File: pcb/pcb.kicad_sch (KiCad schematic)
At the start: 4 parts

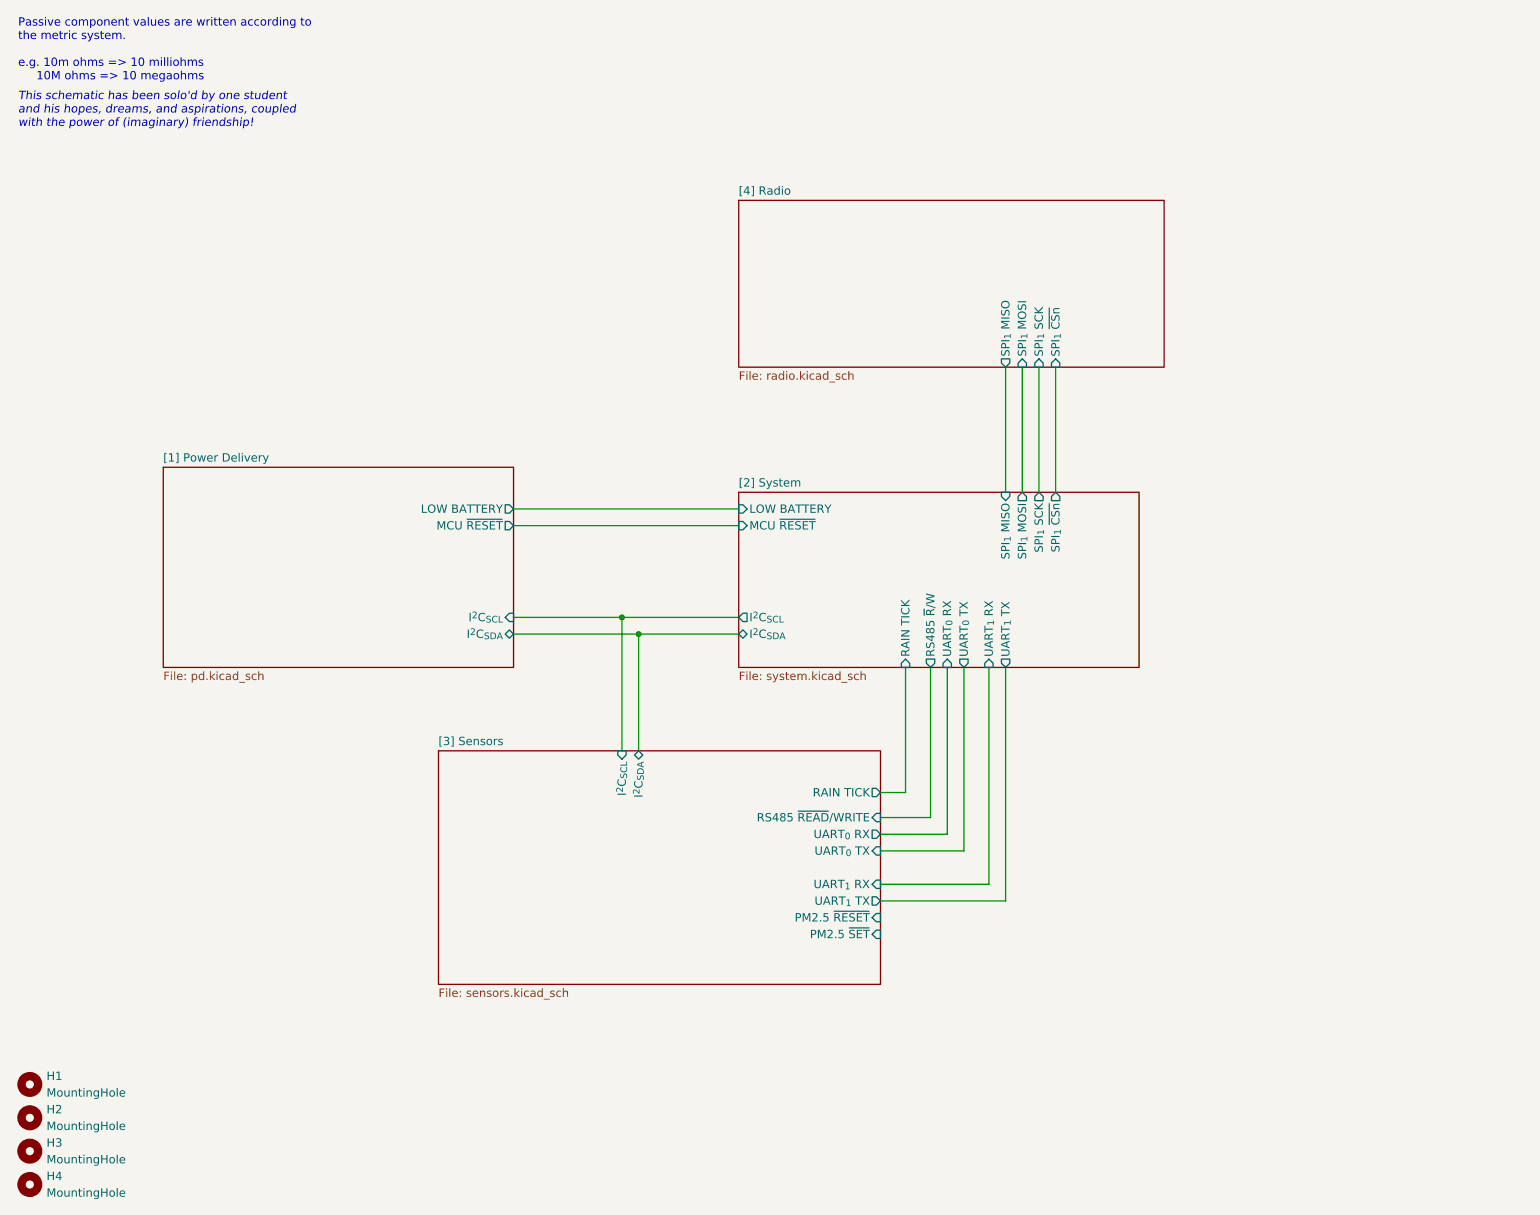
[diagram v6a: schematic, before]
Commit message: feat: added documentation, updated page information
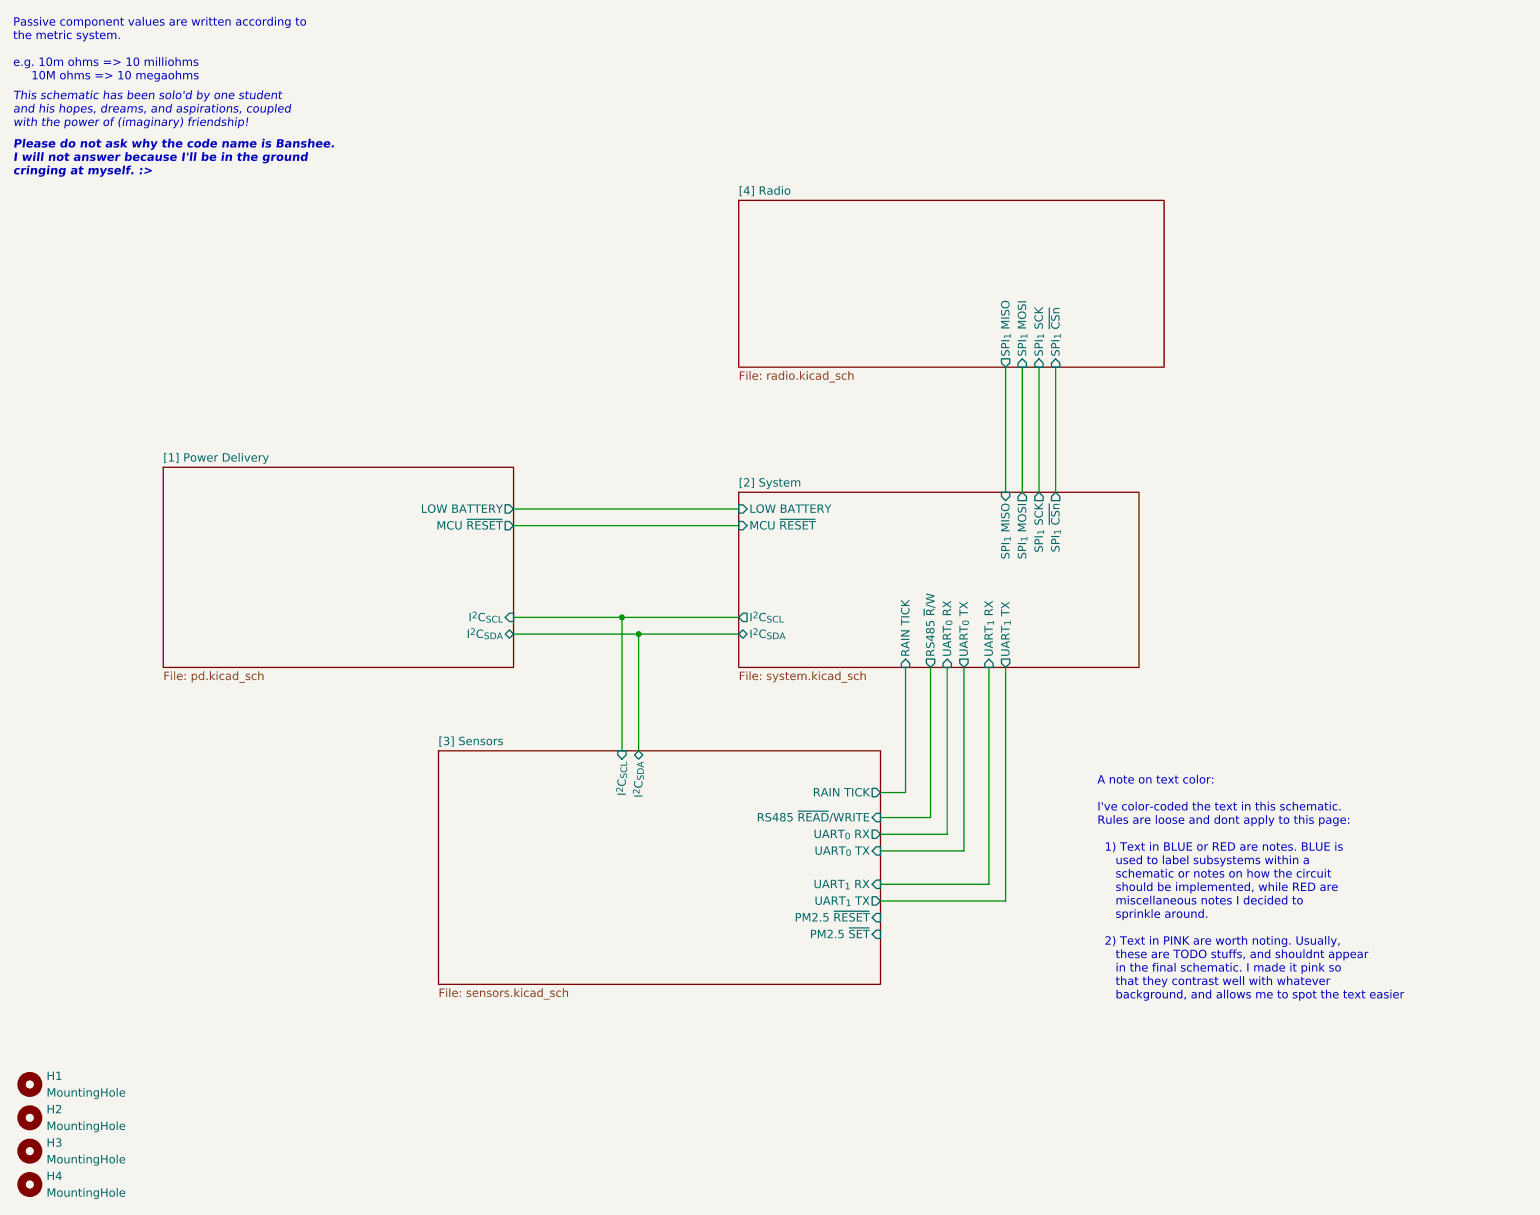
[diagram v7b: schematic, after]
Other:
- note added: "A note on text color: I've color-coded the text in this schematic. Rules are loose and dont apply to this page: 1) Text in BLUE or RED are notes. BLUE is used to label subsystems within a schematic or notes on how the circuit should be implemented, while RED are miscellaneous notes I decided to sprinkle around. 2) Text in PINK are worth noting. Usually, these are TODO stuffs, and shouldnt appear 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"
- note added: "Please do not ask why the code name is Banshee. I will not answer because I'll be in the ground cringing at myself. :>"
- title: Banshee Power Delivery System -> Banshee System Overview
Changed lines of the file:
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@@
 	(paper "A4")
 	(title_block
-		(title "Banshee Power Delivery System")
+		(title "Banshee System Overview")
 		(date "2026-02-26")
 		(rev "1")
@@
 	(text "This schematic has been solo'd by one student\nand his hopes, dreams, and aspirations, coupled\nwith the power of (imaginary) friendship!"
 		(exclude_from_sim no)
-		(at 14.732 29.464 0)
+		(at 13.97 29.464 0)
 		(effects
 			(font
@@
 	(text "Passive component values are written according to\nthe metric system.\n\ne.g. 10m ohms => 10 milliohms\n     10M ohms => 10 megaohms"
 		(exclude_from_sim no)
-		(at 14.732 20.32 0)
+		(at 13.97 20.32 0)
 		(effects
 			(font
@@
 		)
 	)
+	(text "Please do not ask why the code name is Banshee.\nI will not answer because I'll be in the ground\ncringing at myself. :>"
+		(exclude_from_sim no)
+		(at 13.97 36.83 0)
+		(effects
+			(font
+				(size 1.27 1.27)
+				(thickness 0.254)
+				(bold yes)
+				(italic yes)
+				(color 132 0 0 1)
+			)
+			(justify left)
+		)
+	)
+	(text "A note on text color:\n\nI've color-coded the text in this schematic.\nRules are loose and dont apply to this page:\n\n  1) Text in BLUE or RED are notes. BLUE is\n     used to label subsystems within a\n     schematic or notes on how the circuit\n     should be implemented, while RED are \n     miscellaneous notes I decided to \n     sprinkle around.\n\n  2) Text in PINK are worth noting. Usually,\n     these are TODO stuffs, and shouldnt appear\n     in the final schematic. I made it pink so\n     that they contrast well with whatever\n     background, and allows me to spot the text easier"
+		(exclude_from_sim no)
+		(at 179.07 165.1 0)
+		(effects
+			(font
+				(size 1.27 1.27)
+			)
+			(justify left bottom)
+		)
+	)

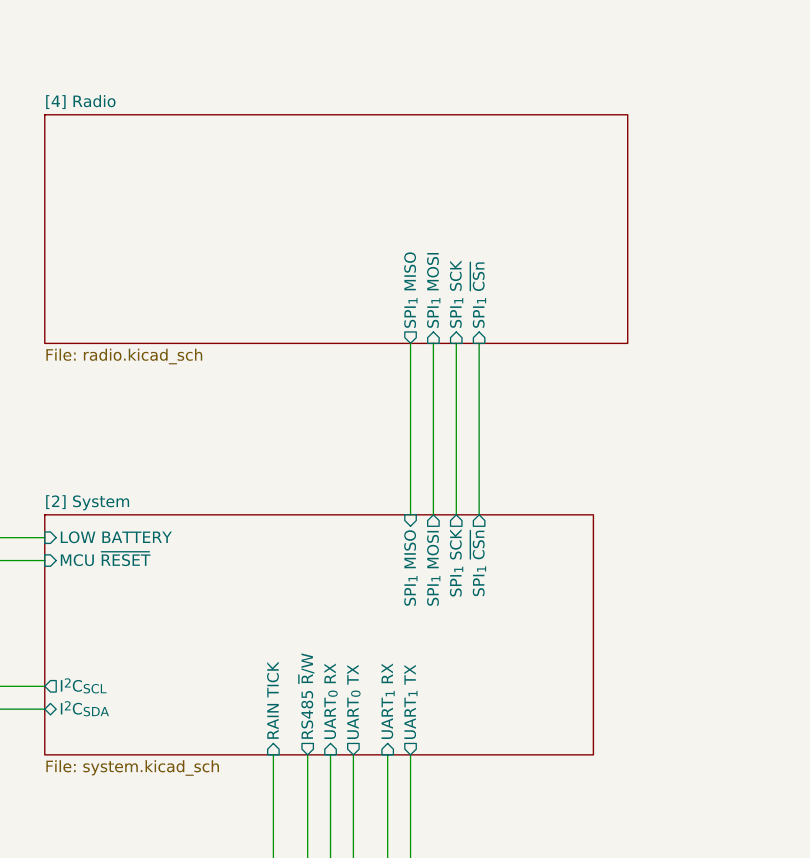
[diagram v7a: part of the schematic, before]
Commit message: feat: sx1278 radio
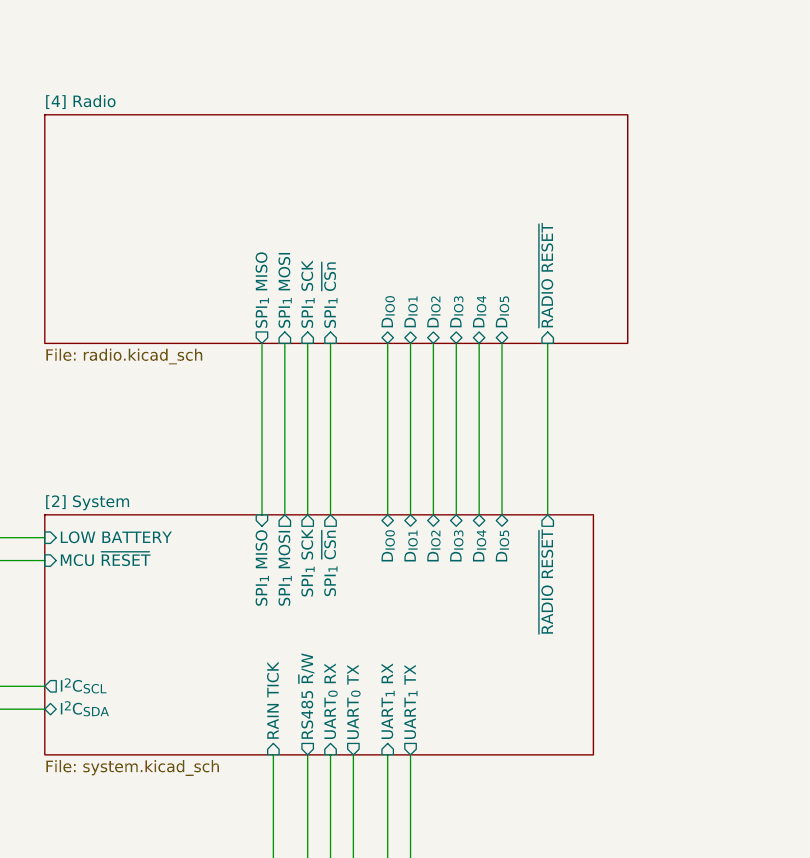
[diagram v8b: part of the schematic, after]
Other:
- sheet [2] System ports: added D_{IO0}, D_{IO1}, D_{IO2}, D_{IO3}, D_{IO4}, D_{IO5}, ~{RADIO RESET}; removed none
- sheet [4] Radio ports: added D_{IO0}, D_{IO1}, D_{IO2}, D_{IO3}, D_{IO4}, D_{IO5}, ~{RADIO RESET}; removed none
